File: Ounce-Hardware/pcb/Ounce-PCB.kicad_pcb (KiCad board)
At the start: 2 copper layers, 135 x 61 mm, 5 parts, among them U1 RaspberryPi_Pico2_W, U2 RaspberryPi_Pico, U3 RaspberryPi_Pico, U4 RaspberryPi_Pico, U5 RaspberryPi_Pico

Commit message: Route ground on pins 3 and 38, hide the other five
Ground is routed as one straight run at y=80.95 from x=89.11 to 210.89. Pins 3
and 38 sit at the same y on opposite pad columns, so the track crosses each
module from one to the other and hops the gap to the next - nine segments, no
vias, continuous copper through both ground pads of all five boards.

GND is now assigned to pins 3 and 38 only. The other five (8, 13, 18, 23, 28)
are the same node inside the Pico, so the netlist demanding they each be wired
was asking for copper that connects nothing new. Their ratlines are gone and
DRC reports no unconnected ground at all, down from 41 items.

16 unconnected remain, all signal: SCK, MOSI, the four chip selects and the
four MISO lines.

Note this is a board-level net assignment. Update PCB from Schematic will put
GND back on all seven pins, as it already did once.

Co-Authored-By: Claude Opus 5 <noreply@anthropic.com>
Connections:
- U1 pad 3: (no net) -> GND
- U2 pad 3: (no net) -> GND
- U3 pad 3: (no net) -> GND
- U4 pad 3: (no net) -> GND
- U5 pad 3: (no net) -> GND
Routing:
- net GND: track 0.00 -> 121.8 mm

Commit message: Add a ground pour on B.Cu
With the within-module p3-p38 segments removed, pin 3 on each board was left
isolated - the only copper was the four hops between modules, and pin 3 relied
on the Pico's internal link, which KiCad's connectivity does not know about.

A B.Cu pour on GND ties every ground pad directly, so both pins on all five
boards are connected in copper rather than through the module. DRC now reports
no unconnected ground at all, and the four inter-module segments become
belt-and-braces rather than the only path.

It also gives the signals a return plane. The bus is 4MHz over about 120mm and
the only return was a single 0.25mm trace along the top margin while the
signals will run along the bottom - a large loop for no reason, when a pour
costs nothing at fab time.

1391mm2 of the 8040mm2 outline is excluded, which is the Pico W antenna
keepouts and pad clearances doing their job: DRC reports zero items_not_allowed,
the same check that caught 24 violations when the keepouts were left behind
during placement.

Thermal reliefs on pads rather than solid connections, so the through-hole
grounds stay hand-solderable.

Co-Authored-By: Claude Opus 5 <noreply@anthropic.com>
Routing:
- net GND: track 121.8 -> 32.9 mm
- added copper zone on B.Cu, net GND
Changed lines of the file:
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@@
-	)
-	(segment
-		(start 167.11 80.95)
-		(end 184.89 80.95)
-		(width 0.25)
-		(layer "F.Cu")
-		(net "GND")
 	)
 	(segment
@@
 	)
 	(segment
-		(start 193.11 80.95)
-		(end 210.89 80.95)
-		(width 0.25)
-		(layer "F.Cu")
-		(net "GND")
-	)
-	(segment
-		(start 115.11 80.95)
-		(end 132.89 80.95)
-		(width 0.25)
-		(layer "F.Cu")
-		(net "GND")
-	)
-	(segment
-		(start 141.11 80.95)
-		(end 158.89 80.95)
-		(width 0.25)
-		(layer "F.Cu")
-		(net "GND")
-	)
-	(segment
-		(start 106.89 80.95)
-		(end 89.11 80.95)
-		(width 0.25)
-		(layer "F.Cu")
-		(net "GND")
-	)
-	(segment
 		(start 132.89 80.95)
 		(end 141.11 80.95)
@@
 		(net "GND")
 	)
+	(zone
+		(net "GND")
+		(layer "B.Cu")
+		(name "GND pour")
+		(hatch edge 0.5)
+		(connect_pads
+			(clearance 0.3)
+		)
+		(min_thickness 0.25)
+		(fill yes
+			(thermal_gap 0.5)
+			(thermal_bridge_width 0.5)
+			(island_removal_mode 0)
+		)
+		(polygon
+			(pts
+				(xy 83 70) (xy 217 70) (xy 217 130) (xy 83 130)
+			)
+		)
+	)
 	(embedded_fonts no)

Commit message: Drop the ground pour, restore the p3-p38 crossings instead
The pour was doing two jobs and only one of them was needed.

As a return plane it was insurance, not a requirement. This bus already runs at
4MHz across a breadboard on jumper wires at 94-100% delivery, and jumper wires
are worse than any trace on this board for loop area and inductance. Nothing in
the current design needs a plane.

The connectivity job was real, but a pour is a heavy way to do it. With the
within-module crossings gone, the chain entered each board at pin 3 and left at
pin 38 through the Pico's internal ground - so unseating one module would have
broken ground for every board downstream, and KiCad flagged those pads because
it cannot see the internal link. Five 17.78mm tracks fix that directly.

Ground is again one continuous run of copper at y=80.95 from x=89.11 to 210.89
through both ground pads of all five boards. DRC reports no unconnected ground,
same as with the pour, and the board keeps a clear B.Cu layer for routing the
sixteen signal connections.

Worth revisiting only if the SPI clock goes up.

Co-Authored-By: Claude Opus 5 <noreply@anthropic.com>
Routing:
- net GND: track 32.9 -> 121.8 mm
- removed copper zone on B.Cu, net GND
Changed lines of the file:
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@@
+	)
+	(segment
+		(start 115.11 80.95)
+		(end 132.89 80.95)
+		(width 0.25)
+		(layer "F.Cu")
+		(net "GND")
+	)
+	(segment
+		(start 167.11 80.95)
+		(end 184.89 80.95)
+		(width 0.25)
+		(layer "F.Cu")
+		(net "GND")
+	)
+	(segment
+		(start 193.11 80.95)
+		(end 210.89 80.95)
+		(width 0.25)
+		(layer "F.Cu")
+		(net "GND")
 	)
 	(segment
@@
 	)
 	(segment
+		(start 89.11 80.95)
+		(end 106.89 80.95)
+		(width 0.25)
+		(layer "F.Cu")
+		(net "GND")
+	)
+	(segment
+		(start 141.11 80.95)
+		(end 158.89 80.95)
+		(width 0.25)
+		(layer "F.Cu")
+		(net "GND")
+	)
+	(segment
 		(start 132.89 80.95)
 		(end 141.11 80.95)
@@
 		(net "GND")
 	)
-	(zone
-		(net "GND")
-		(layer "B.Cu")
-		(name "GND pour")
-		(hatch edge 0.5)
-		(connect_pads
-			(clearance 0.3)
-		)
-		(min_thickness 0.25)
-		(fill yes
-			(thermal_gap 0.5)
-			(thermal_bridge_width 0.5)
-			(island_removal_mode 0)
-		)
-		(polygon
-			(pts
-				(xy 83 70) (xy 217 70) (xy 217 130) (xy 83 130)
-			)
-		)
-	)
 	(embedded_fonts no)

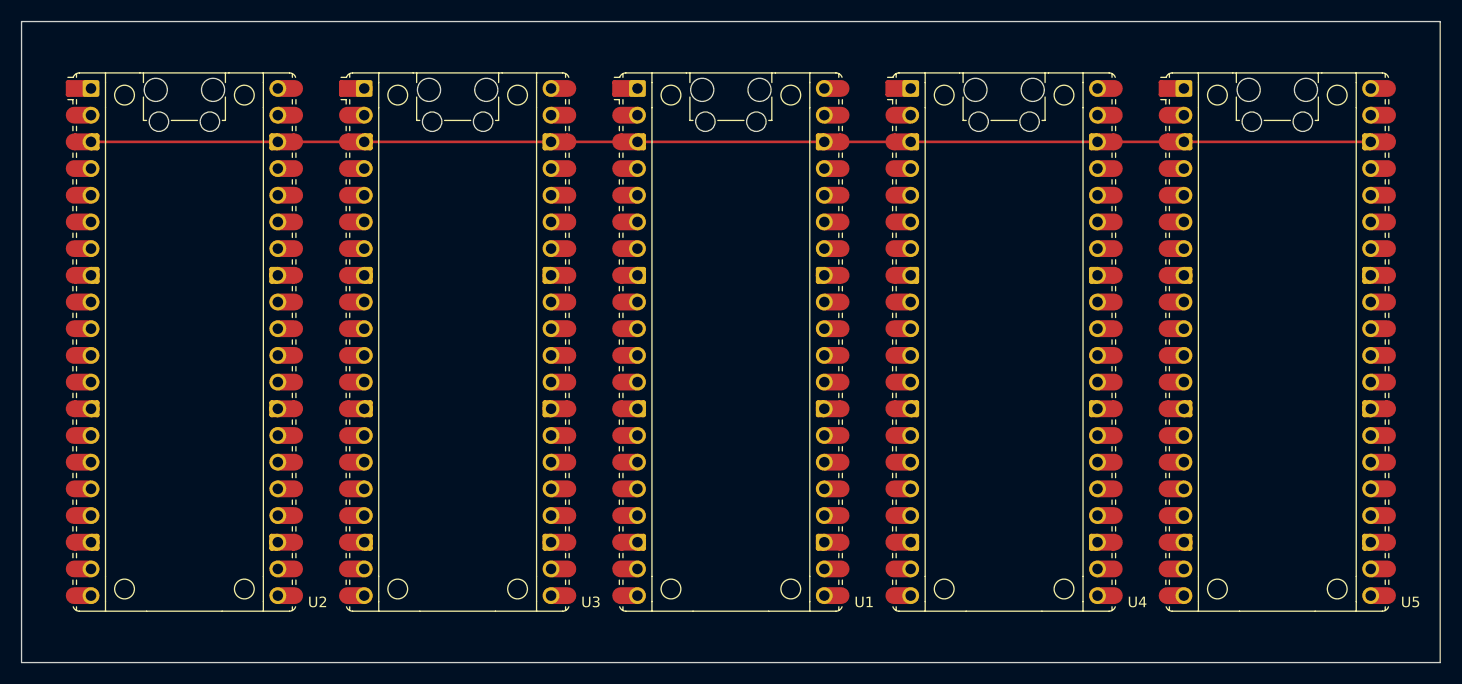
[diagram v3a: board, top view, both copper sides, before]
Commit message: Enforce a real clearance rule, drop a leftover stub
The routing is complete - 0 unconnected, 104 segments, 763mm of copper - and
every net matches spi_master.cpp pin for pin.

Two things it was hiding. Min clearance was set to 0.000mm, so DRC was not
checking spacing at all and a clean report meant very little. Probing shows the
routing actually holds 0.20mm everywhere and only fails at 0.25mm, which is
comfortably manufacturable, so the rule is now set to 0.20 and DRC has
something to enforce.

Also removed a dangling 0.5mm MOSI stub at (152.5, 126.625) with one end
connected to nothing - stray click while routing, harmless at this speed but
not worth fabricating.

DRC is now clean apart from the five lib_footprint_mismatch warnings, which are
local-override notices rather than geometry.

Co-Authored-By: Claude Opus 5 <noreply@anthropic.com>
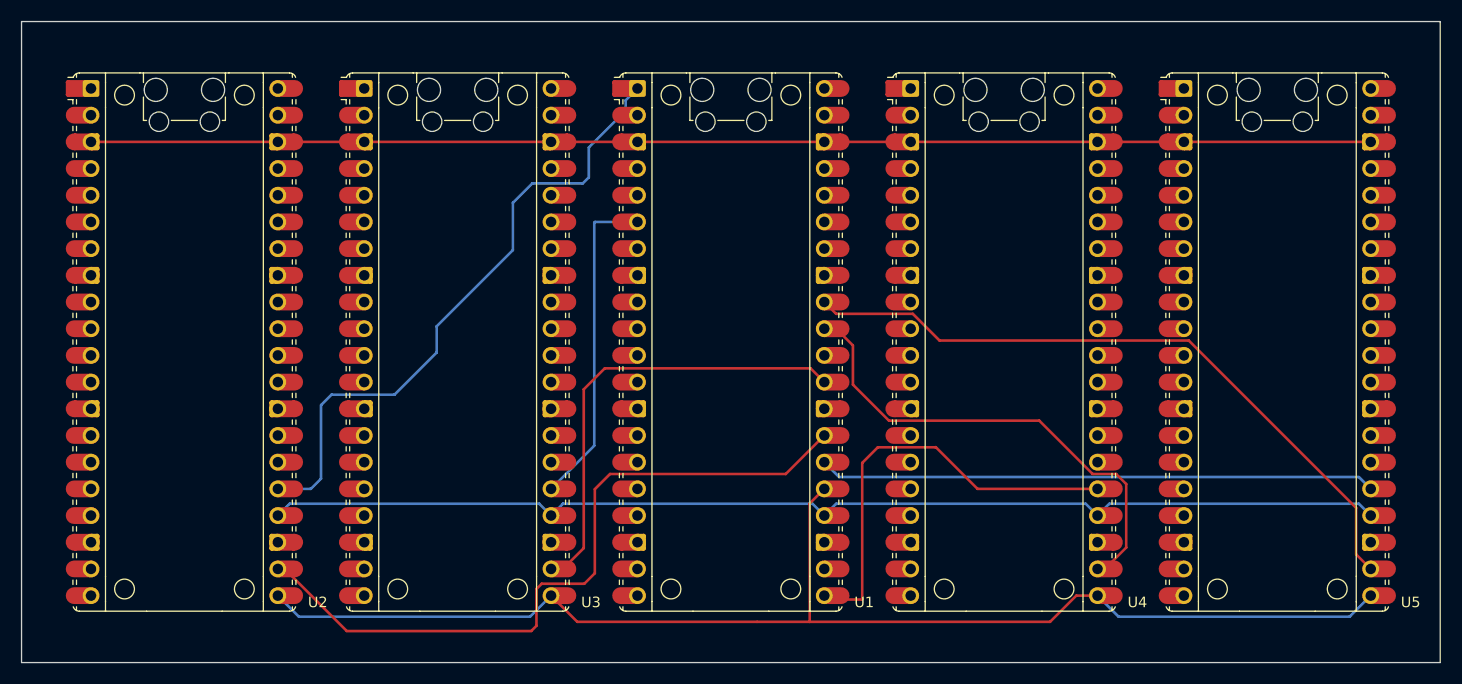
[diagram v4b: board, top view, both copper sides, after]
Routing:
- net SPI0_MOSI: track 0.00 -> 122.6 mm
- net SPI0_SCK: track 0.00 -> 107.7 mm
- net SPI0_CS0: track 0.00 -> 68.9 mm
- net SPI0_CS3: track 0.00 -> 65.1 mm
- net SPI0_MISO0: track 0.00 -> 60.4 mm
- net SPI0_MISO3: track 0.00 -> 53.1 mm
- net SPI0_CS2: track 0.00 -> 46.7 mm
- net SPI0_CS1: track 0.00 -> 43.3 mm
- net SPI0_MISO2: track 0.00 -> 42.3 mm
- net SPI0_MISO1: track 0.00 -> 31.2 mm

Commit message: Silkscreen OUNCE THE TITAN SLAYER on the back
Four rows on B.SilkS down the middle of the modules:

    O    U    N    C    E
              THE
    T    I    T    A    N
            SLAYER

Letters are assigned by descending board x, not ascending. Text on a back layer
is mirrored, so the module at x=202 is the leftmost one you see when the board
is flipped over - putting O there and E on x=98 is what makes it read forwards.
THE and SLAYER sit on U1, which is the middle module from either side.

Placed in the strip between each module's two pad columns. That looked too
narrow at first: the footprint has six pad columns, not two, leaving under 4mm.
But the four inner pads are all debug pads at the top (y 76 and 79), so below
that the middle is clear for 15.58mm - room to spare for 10mm-wide glyphs.

Rows at y 86, 97, 109 and 119.5. Spacing came from ink extents rather than
KiCad's text bounding boxes, which pad a 9mm glyph out to 15.4mm and made four
rows look impossible; measured edge to edge the gaps are 2.15 to 3.30mm and the
block spans 80.80..122.65 inside the 80.2..123.0 clear strip.

DRC unchanged: 0 unconnected, and all ten signal nets still match the schematic.

Co-Authored-By: Claude Opus 5 <noreply@anthropic.com>
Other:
- board text added: "A"
- board text added: "C"
- board text added: "E"
- board text added: "I"
- board text added: "N"
- board text added: "O"
- board text added: "SLAYER"
- board text added: "T"
- board text added: "THE"
- board text added: "U"
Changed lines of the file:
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@@
 		(layer "Edge.Cuts")
+	)
+	(gr_text "SLAYER"
+		(at 150 119.5 0)
+		(layer "B.SilkS")
+		(effects
+			(font
+				(size 5.5 2.2)
+				(thickness 0.8)
+			)
+			(justify mirror)
+		)
+	)
+	(gr_text "THE"
+		(at 150 97 0)
+		(layer "B.SilkS")
+		(effects
+			(font
+				(size 6 4)
+				(thickness 1)
+			)
+			(justify mirror)
+		)
+	)
+	(gr_text "E"
+		(at 98 86 0)
+		(layer "B.SilkS")
+		(effects
+			(font
+				(size 9 7)
+				(thickness 1.4)
+			)
+			(justify mirror)
+		)
+	)
+	(gr_text "N"
+		(at 98 109 0)
+		(layer "B.SilkS")
+		(effects
+			(font
+				(size 9 7)
+				(thickness 1.4)
+			)
+			(justify mirror)
+		)
+	)
+	(gr_text "C"
+		(at 124 86 0)
+		(layer "B.SilkS")
+		(effects
+			(font
+				(size 9 7)
+				(thickness 1.4)
+			)
+			(justify mirror)
+		)
+	)
+	(gr_text "A"
+		(at 124 109 0)
+		(layer "B.SilkS")
+		(effects
+			(font
+				(size 9 7)
+				(thickness 1.4)
+			)
+			(justify mirror)
+		)
+	)
+	(gr_text "N"
+		(at 150 86 0)
+		(layer "B.SilkS")
+		(effects
+			(font
+				(size 9 7)
+				(thickness 1.4)
+			)
+			(justify mirror)
+		)
+	)
+	(gr_text "T"
+		(at 150 109 0)
+		(layer "B.SilkS")
+		(effects
+			(font
+				(size 9 7)
+				(thickness 1.4)
+			)
+			(justify mirror)
+		)
+	)
+	(gr_text "U"
+		(at 176 86 0)
+		(layer "B.SilkS")
+		(effects
+			(font
+				(size 9 7)
+				(thickness 1.4)
+			)
+			(justify mirror)
+		)
+	)
+	(gr_text "I"
+		(at 176 109 0)
+		(layer "B.SilkS")
+		(effects
+			(font
+				(size 9 7)
+				(thickness 1.4)
+			)
+			(justify mirror)
+		)
+	)
+	(gr_text "O"
+		(at 202 86 0)
+		(layer "B.SilkS")
+		(effects
+			(font
+				(size 9 7)
+				(thickness 1.4)
+			)
+			(justify mirror)
+		)
+	)
+	(gr_text "T"
+		(at 202 109 0)
+		(layer "B.SilkS")
+		(effects
+			(font
+				(size 9 7)
+				(thickness 1.4)
+			)
+			(justify mirror)
+		)
 	)
 	(segment

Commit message: Add the designer credit and even out the silkscreen spacing
"designed by emmanuel roy :)" on B.SilkS in the bottom-left corner as seen from
the back, which is high board x - the same mirroring that decides the letter
order above it.

Also evened the four text rows. They were at 86 / 97 / 109 / 119.5 with gaps of
2.30, 3.30 and 2.15mm; now at 85.400 / 97.000 / 108.600 / 119.850, which is an
exact 2.900mm between every pair, derived from each row's ink height rather
than eyeballed.

The credit is centred in the 4.97mm band between the last pad row and the board
edge, clearing pads by 0.79mm and the edge by 1.09mm, with a 2.00mm side
margin. Aiming for a 2mm bottom margin instead put it 0.42mm from the pads,
because the real bounding box is 3.39mm tall against the 2.30mm the glyph
height suggests.

All five rows verified: the four word rows sit exactly on module centres, the
credit is the only thing off-centre and deliberately so. DRC unchanged.

Co-Authored-By: Claude Opus 5 <noreply@anthropic.com>
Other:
- board text added: "designed by emmanuel roy :)"
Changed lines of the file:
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@@
 		(layer "Edge.Cuts")
 	)
+	(gr_text "designed by emmanuel roy :)"
+		(at 200.632383 127.715 0)
+		(layer "B.SilkS")
+		(effects
+			(font
+				(size 2 1.3)
+				(thickness 0.3)
+			)
+			(justify mirror)
+		)
+	)
 	(gr_text "SLAYER"
-		(at 150 119.5 0)
+		(at 150 119.85 0)
 		(layer "B.SilkS")
 		(effects
@@
 	)
 	(gr_text "E"
-		(at 98 86 0)
+		(at 98 85.4 0)
 		(layer "B.SilkS")
 		(effects
@@
 	)
 	(gr_text "N"
-		(at 98 109 0)
+		(at 98 108.6 0)
 		(layer "B.SilkS")
 		(effects
@@
 	)
 	(gr_text "C"
-		(at 124 86 0)
+		(at 124 85.4 0)
 		(layer "B.SilkS")
 		(effects
@@
 	)
 	(gr_text "A"
-		(at 124 109 0)
+		(at 124 108.6 0)
 		(layer "B.SilkS")
 		(effects
@@
 	)
 	(gr_text "N"
-		(at 150 86 0)
+		(at 150 85.4 0)
 		(layer "B.SilkS")
 		(effects
@@
 	)
 	(gr_text "T"
-		(at 150 109 0)
+		(at 150 108.6 0)
 		(layer "B.SilkS")
 		(effects
@@
 	)
 	(gr_text "U"
-		(at 176 86 0)
+		(at 176 85.4 0)
 		(layer "B.SilkS")
 		(effects
@@
 	)
 	(gr_text "I"
-		(at 176 109 0)
+		(at 176 108.6 0)
 		(layer "B.SilkS")
 		(effects
@@
 	)
 	(gr_text "O"
-		(at 202 86 0)
+		(at 202 85.4 0)
 		(layer "B.SilkS")
 		(effects
@@
 	)
 	(gr_text "T"
-		(at 202 109 0)
+		(at 202 108.6 0)
 		(layer "B.SilkS")
 		(effects
